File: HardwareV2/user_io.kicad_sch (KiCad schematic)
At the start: 7 parts, among them J1 Conn_01x08_MountingPin, SW2 1825910-6, SW3 1825910-6, SW4 1825910-6, SW5 1825910-6, U7 PEC12R-4215F-S0024, U8 PEC12R-4215F-S0024

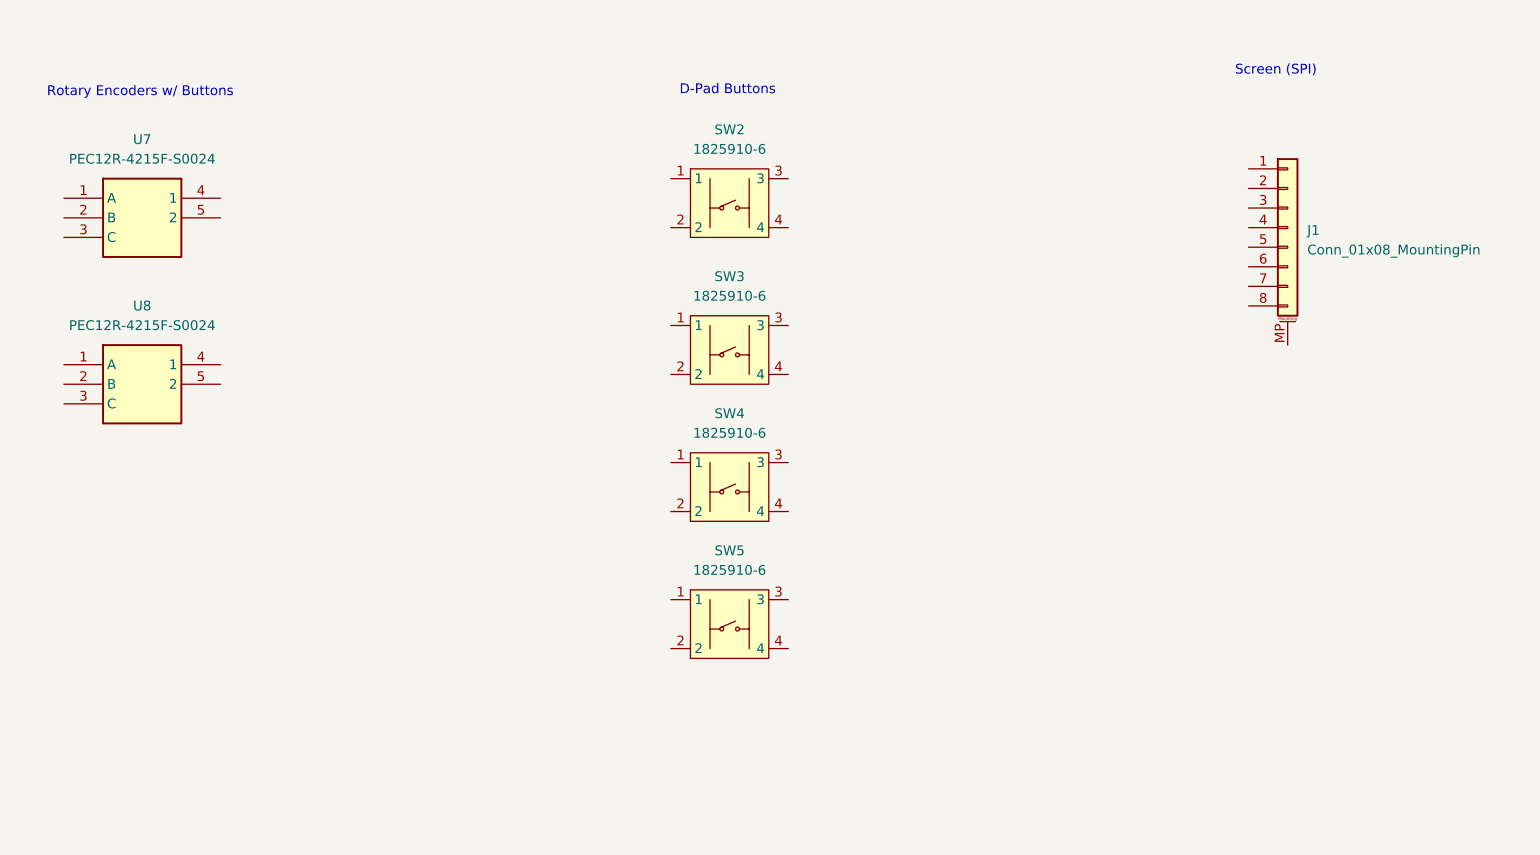
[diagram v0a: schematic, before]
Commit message: initial v2 pcb layout minus passives
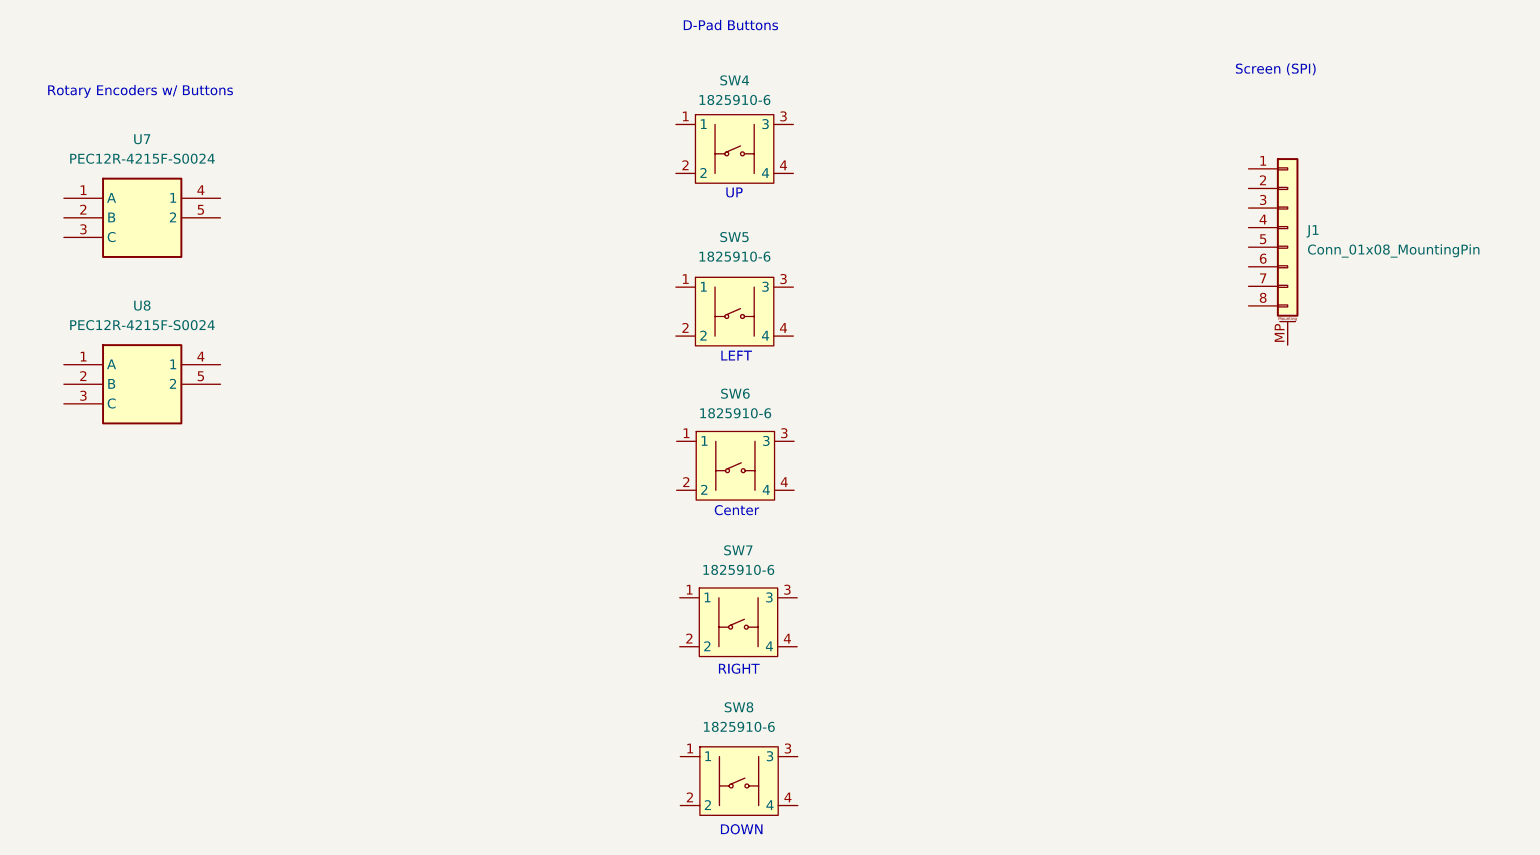
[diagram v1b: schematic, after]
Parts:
- added SW8: 1825910-6, RP2350b_parts_layout:SW-TH_4P-L6.0-W6.0-P4.50-LS6.5, symbol RP2350b_part_sch:1825910-6
- SW4: renamed from SW2; footprint parts_lib:SW-TH_4P-L6.0-W6.0-P4.50-LS6.5 -> RP2350b_parts_layout:SW-TH_4P-L6.0-W6.0-P4.50-LS6.5
- SW5: renamed from SW3; footprint parts_lib:SW-TH_4P-L6.0-W6.0-P4.50-LS6.5 -> RP2350b_parts_layout:SW-TH_4P-L6.0-W6.0-P4.50-LS6.5
- SW6: renamed from SW4; footprint parts_lib:SW-TH_4P-L6.0-W6.0-P4.50-LS6.5 -> RP2350b_parts_layout:SW-TH_4P-L6.0-W6.0-P4.50-LS6.5
- SW7: renamed from SW5; footprint parts_lib:SW-TH_4P-L6.0-W6.0-P4.50-LS6.5 -> RP2350b_parts_layout:SW-TH_4P-L6.0-W6.0-P4.50-LS6.5
- U7, U8: footprint PEC12R-4XXXF-SXXXX_1 -> RP2350b_parts_layout:PEC12R-4XXXF-SXXXX_1
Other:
- note added: "Center"
- note added: "DOWN"
- note added: "LEFT"
- note added: "RIGHT"
- note added: "UP"
- moved on the sheet: SW4, SW5, SW6, SW7
